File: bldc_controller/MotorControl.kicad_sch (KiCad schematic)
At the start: 10 parts, among them U10 DRV8353FS

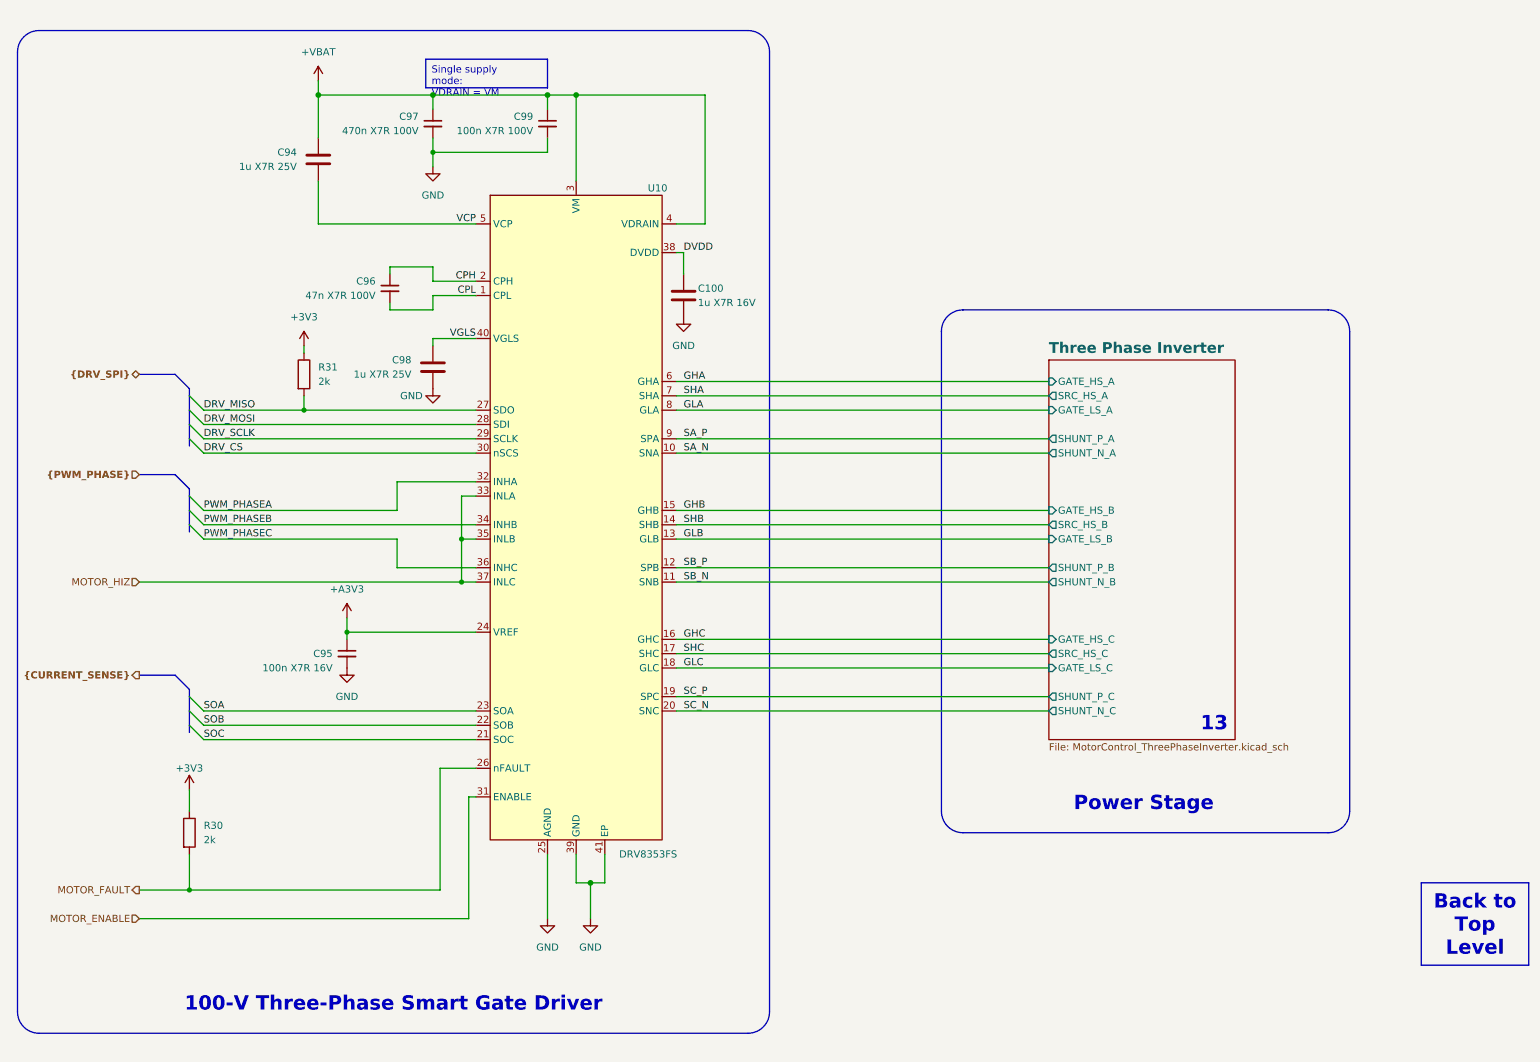
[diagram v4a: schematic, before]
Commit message: Added TVS diodes to all interfaces
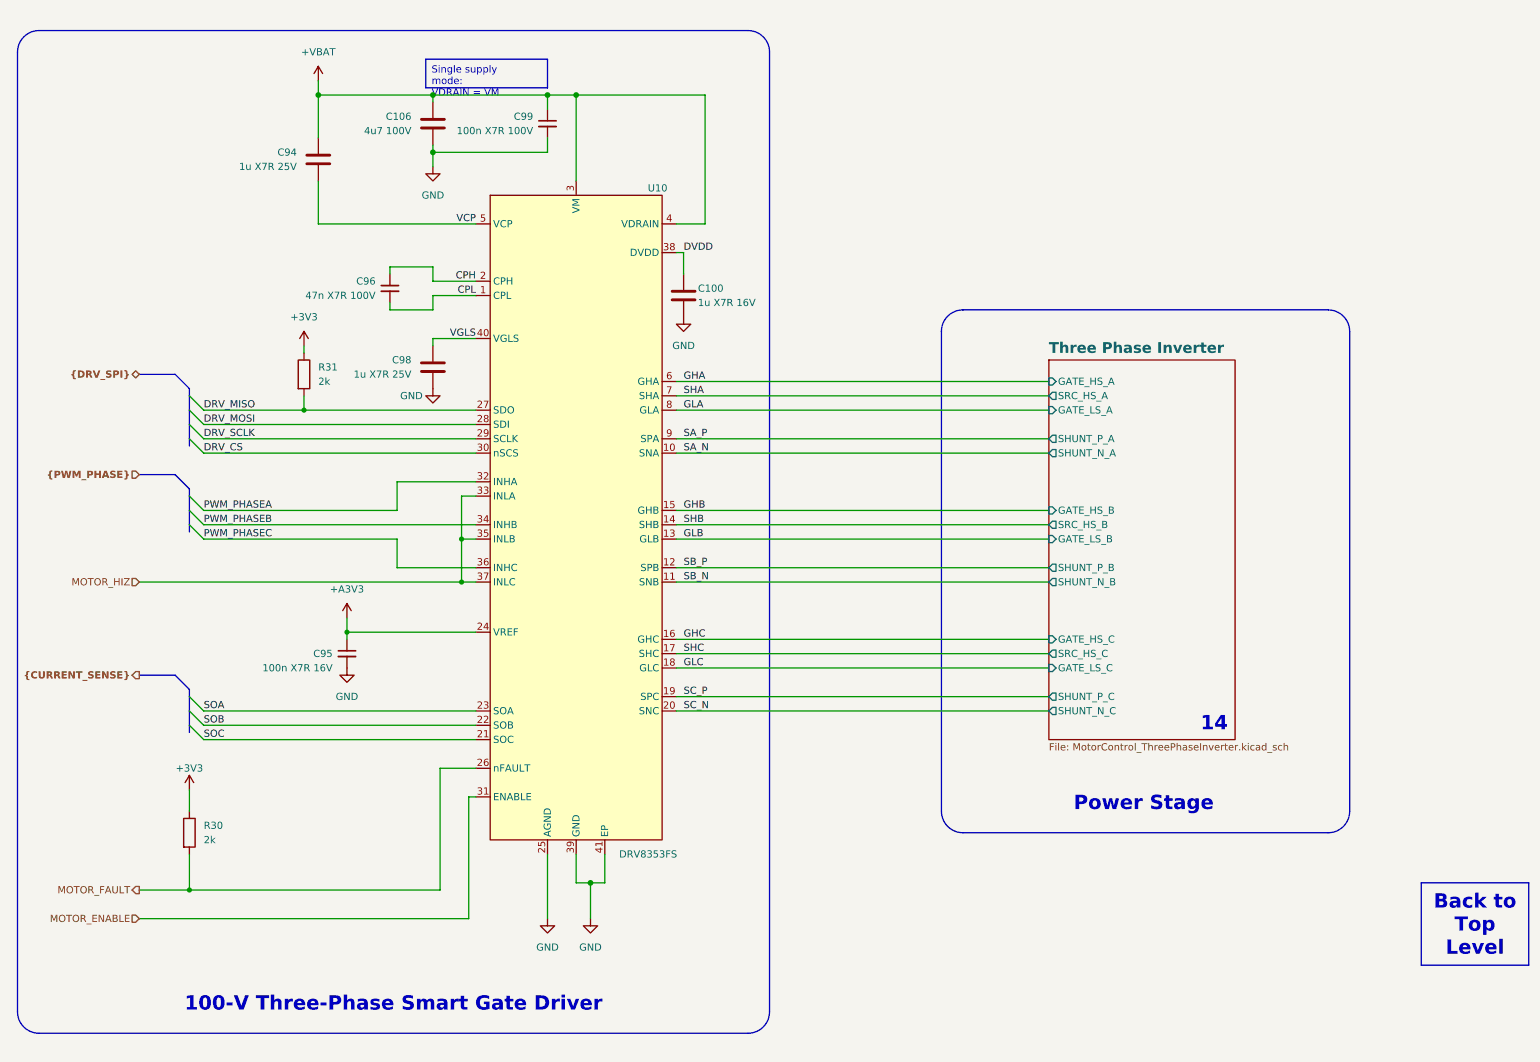
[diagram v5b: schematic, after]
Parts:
- removed C97: 470n X7R 100V, 0_capacitor_smd:C_0402_1005_DensityHigh, symbol Device:C_Small
- added C106: 4u7 100V, 0_capacitor_smd:C_1206_3216_DensityHighest, symbol Device:C
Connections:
- net +VBAT: now also C106.1
- net GND: now also C106.2
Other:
- note added: "14"
- note removed: "13"
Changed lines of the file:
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@@
     (comment 3 "Author: Vincent Nguyen")
   )
+  (junction (at 90.17 36.83) (diameter 1.016) (color 0 0 0 1)
+  )
   (junction (at 110.49 26.67) (diameter 1.016) (color 200 50 50 1)
   )
+  (junction (at 90.17 26.67) (diameter 1.016) (color 200 50 50 1)
+  )
   (junction (at 115.57 26.67) (diameter 1.016) (color 200 50 50 1)
   )
-  (junction (at 90.17 36.83) (diameter 0) (color 0 0 0 1)
-  )
   (junction (at 118.11 166.37) (diameter 1.016) (color 0 0 0 1)
   )
@@
   )
   (junction (at 74.93 121.92) (diameter 0) (color 0 0 0 0)
-  )
-  (junction (at 90.17 26.67) (diameter 1.016) (color 200 50 50 1)
   )
   (junction (at 95.25 105.41) (diameter 0) (color 0 0 0 0)
@@
     (stroke (width 0) (type default))
   )
-  (wire (pts (xy 90.17 36.83) (xy 90.17 34.29))
-    (stroke (width 0.381) (type default) (color 0 0 0 1))
-  )
   (wire (pts (xy 46.99 161.29) (xy 46.99 167.64))
     (stroke (width 0) (type default))
+  )
+  (wire (pts (xy 90.17 26.67) (xy 90.17 27.94))
+    (stroke (width 0.381) (type default) (color 200 50 50 1))
   )
   (wire (pts (xy 96.52 172.72) (xy 96.52 151.13))
@@
     (stroke (width 0) (type default))
   )
-  (wire (pts (xy 90.17 26.67) (xy 90.17 29.21))
+  (wire (pts (xy 90.17 26.67) (xy 110.49 26.67))
     (stroke (width 0.381) (type default) (color 200 50 50 1))
   )
@@
     (stroke (width 0) (type default))
   )
-  (wire (pts (xy 69.85 26.67) (xy 90.17 26.67))
-    (stroke (width 0.381) (type default) (color 200 50 50 1))
+  (wire (pts (xy 90.17 36.83) (xy 90.17 35.56))
+    (stroke (width 0.381) (type default) (color 0 0 0 1))
   )
   (wire (pts (xy 49.53 90.17) (xy 97.79 90.17))
@@
     (stroke (width 0) (type default))
   )
-  (wire (pts (xy 90.17 39.37) (xy 90.17 36.83))
+  (wire (pts (xy 90.17 36.83) (xy 90.17 39.37))
     (stroke (width 0.381) (type default) (color 0 0 0 1))
   )
@@
     (stroke (width 0) (type default))
   )
-  (wire (pts (xy 90.17 26.67) (xy 110.49 26.67))
+  (wire (pts (xy 69.85 26.67) (xy 90.17 26.67))
     (stroke (width 0.381) (type default) (color 200 50 50 1))
   )
@@
     (effects (font (size 2.54 2.54) (thickness 0.508) bold (color 0 0 0 1)) (justify bottom))
   )
-  (text "13" (at 231.14 139.7 0)
-    (effects (font (size 2.54 2.54) bold (color 100 30 50 1)) (justify right bottom) (href "#13"))
+  (text "14" (at 231.14 139.7 0)
+    (effects (font (size 2.54 2.54) bold (color 100 30 50 1)) (justify right bottom) (href "#14"))
   )
   (label "DRV_MOSI" (at 49.53 85.09 0) (fields_autoplaced)
@@
         (path "/0650c7a8-acba-429c-9f8e-eec0baf0bc1c/a6223e2e-2896-4182-b4ad-55a63bc87f3d"
           (reference "#PWR061") (unit 1)
+        )
+      )
+    )
+  )
+  (symbol (lib_id "Device:C") (at 90.17 31.75 0) (mirror y) (unit 1)
+    (in_bom yes) (on_board yes) (dnp no)
+    (property "Reference" "C106" (at 86.36 30.48 0)
+      (effects (font (size 1.27 1.27)) (justify left))
+    )
+    (property "Value" "4u7 100V" (at 86.36 33.02 0)
+      (effects (font (size 1.27 1.27)) (justify left))
+    )
+    (property "Footprint" "0_capacitor_smd:C_1206_3216_DensityHighest" (at 89.2048 35.56 0)
+      (effects (font (size 1.27 1.27)) hide)
+    )
+    (property "Datasheet" "~" (at 90.17 31.75 0)
+      (effects (font (size 1.27 1.27)) hide)
+    )
+    (pin "1")
+    (pin "2")
+    (instances
+      (project "bldc_controller"
+        (path "/0650c7a8-acba-429c-9f8e-eec0baf0bc1c/a6223e2e-2896-4182-b4ad-55a63bc87f3d/4a9c9b06-3536-46ef-a76d-6cac03a1fe38"
+          (reference "C106") (unit 1)
+        )
+        (path "/0650c7a8-acba-429c-9f8e-eec0baf0bc1c/a6223e2e-2896-4182-b4ad-55a63bc87f3d"
+          (reference "C97") (unit 1)
         )
       )
@@
     )
   )
-  (symbol (lib_id "Device:C_Small") (at 90.17 31.75 0) (mirror y) (unit 1)
-    (in_bom yes) (on_board yes) (dnp no)
-    (property "Reference" "C97" (at 87.63 30.48 0)
-      (effects (font (size 1.27 1.27)) (justify left))
-    )
-    (property "Value" "470n X7R 100V" (at 87.63 33.02 0)
-      (effects (font (size 1.27 1.27)) (justify left))
-    )
-    (property "Footprint" "0_capacitor_smd:C_0402_1005_DensityHigh" (at 90.17 31.75 0)
-      (effects (font (size 1.27 1.27)) hide)
-    )
-    (property "Datasheet" "~" (at 90.17 31.75 0)
-      (effects (font (size 1.27 1.27)) hide)
-    )
-    (pin "1")
-    (pin "2")
-    (instances
-      (project "bldc_controller"
-        (path "/0650c7a8-acba-429c-9f8e-eec0baf0bc1c/a6223e2e-2896-4182-b4ad-55a63bc87f3d"
-          (reference "C97") (unit 1)
-        )
-      )
-    )
-  )
   (symbol (lib_id "Device:R") (at 67.31 76.2 0) (unit 1)
     (in_bom yes) (on_board yes) (dnp no) (fields_autoplaced)
@@
     (instances
       (project "bldc_controller"
-        (path "/0650c7a8-acba-429c-9f8e-eec0baf0bc1c/a6223e2e-2896-4182-b4ad-55a63bc87f3d" (page "13"))
-      )
-    )
+        (path "/0650c7a8-acba-429c-9f8e-eec0baf0bc1c/a6223e2e-2896-4182-b4ad-55a63bc87f3d" (page "14"))
+      )
+    )

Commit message: might have fixed net issue, added dxf and svgs
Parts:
- renumbered C106 to C97
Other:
- sheet Three Phase Inverter renamed Motor Control - Inverter
- note added: "Page 9"
- note removed: "14"
- moved on the sheet: C100, C94, C95, C96, C97, C98, C99, R30, R31, U10

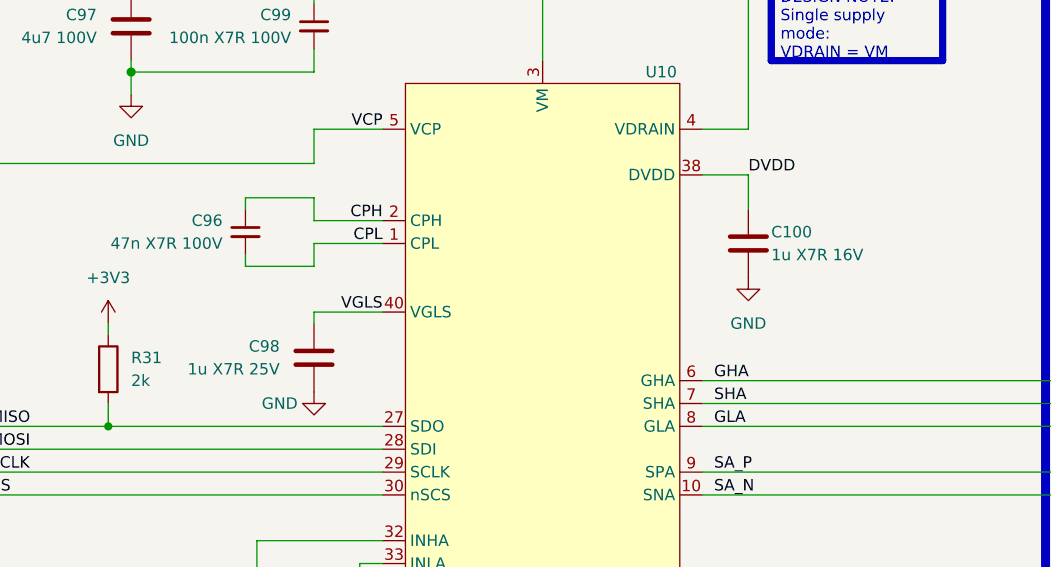
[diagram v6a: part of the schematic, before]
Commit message: added chassis connection to connector MP. Might need to change design rules to be compatible with low-cost PCBWay
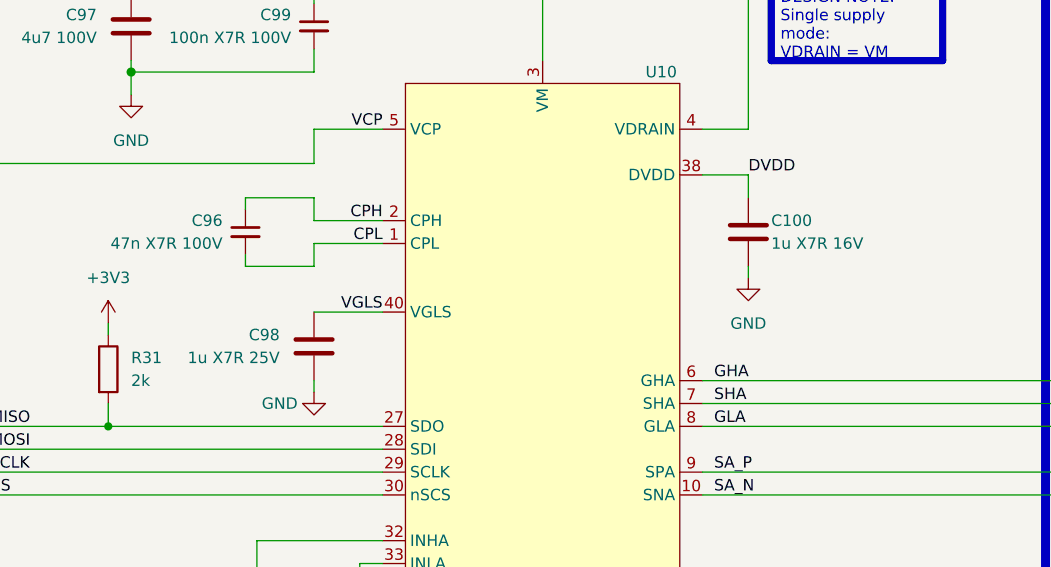
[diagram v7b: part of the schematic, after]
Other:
- moved on the sheet: C100, C98
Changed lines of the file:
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@@
     (stroke (width 0) (type default))
+  )
+  (wire (pts (xy 138.43 72.39) (xy 138.43 73.66))
+    (stroke (width 0.381) (type default) (color 0 0 0 1))
   )
   (wire (pts (xy 49.53 60.96) (xy 90.17 60.96))
@@
   )
   (wire (pts (xy 110.49 168.91) (xy 110.49 173.99))
-    (stroke (width 0) (type default))
+    (stroke (width 0.381) (type default) (color 0 0 0 1))
   )
   (wire (pts (xy 46.99 165.1) (xy 46.99 168.91))
@@
     (stroke (width 0.381) (type default) (color 200 50 50 1))
   )
-  (wire (pts (xy 138.43 66.04) (xy 138.43 62.23))
+  (wire (pts (xy 138.43 64.77) (xy 138.43 62.23))
     (stroke (width 0) (type default))
   )
@@
     (stroke (width 0) (type default))
   )
-  (wire (pts (xy 90.17 78.74) (xy 90.17 77.47))
-    (stroke (width 0) (type default))
-  )
   (wire (pts (xy 82.55 64.77) (xy 82.55 66.04))
     (stroke (width 0) (type default))
@@
   (bus (pts (xy 46.99 140.97) (xy 46.99 143.51))
     (stroke (width 0) (type default))
+  )
+  (wire (pts (xy 90.17 85.09) (xy 90.17 86.36))
+    (stroke (width 0.381) (type default) (color 0 0 0 1))
   )
   (bus (pts (xy 44.45 101.6) (xy 38.1 101.6))
@@
     )
   )
-  (symbol (lib_id "Device:C") (at 90.17 82.55 0) (mirror y) (unit 1)
+  (symbol (lib_id "Device:C") (at 90.17 81.28 0) (mirror y) (unit 1)
     (in_bom yes) (on_board yes) (dnp no)
-    (property "Reference" "C98" (at 86.36 81.28 0)
-      (effects (font (size 1.27 1.27)) (justify left))
-    )
-    (property "Value" "1u X7R 25V" (at 86.36 83.82 0)
-      (effects (font (size 1.27 1.27)) (justify left))
-    )
-    (property "Footprint" "0_capacitor_smd:C_0402_1005_DensityHigh" (at 89.2048 86.36 0)
-      (effects (font (size 1.27 1.27)) hide)
-    )
-    (property "Datasheet" "~" (at 90.17 82.55 0)
+    (property "Reference" "C98" (at 86.36 80.01 0)
+      (effects (font (size 1.27 1.27)) (justify left))
+    )
+    (property "Value" "1u X7R 25V" (at 86.36 82.55 0)
+      (effects (font (size 1.27 1.27)) (justify left))
+    )
+    (property "Footprint" "0_capacitor_smd:C_0402_1005_DensityHigh" (at 89.2048 85.09 0)
+      (effects (font (size 1.27 1.27)) hide)
+    )
+    (property "Datasheet" "~" (at 90.17 81.28 0)
       (effects (font (size 1.27 1.27)) hide)
     )
@@
     )
   )
-  (symbol (lib_id "Device:C") (at 138.43 69.85 0) (unit 1)
+  (symbol (lib_id "Device:C") (at 138.43 68.58 0) (unit 1)
     (in_bom yes) (on_board yes) (dnp no)
-    (property "Reference" "C100" (at 140.97 68.58 0)
-      (effects (font (size 1.27 1.27)) (justify left))
-    )
-    (property "Value" "1u X7R 16V" (at 140.97 71.12 0)
-      (effects (font (size 1.27 1.27)) (justify left))
-    )
-    (property "Footprint" "0_capacitor_smd:C_0402_1005_DensityHigh" (at 139.3952 73.66 0)
-      (effects (font (size 1.27 1.27)) hide)
-    )
-    (property "Datasheet" "~" (at 138.43 69.85 0)
-      (effects (font (size 1.27 1.27)) hide)
-    )
+    (property "Reference" "C100" (at 140.97 67.31 0)
+      (effects (font (size 1.27 1.27)) (justify left))
+    )
+    (property "Value" "1u X7R 16V" (at 140.97 69.85 0)
+      (effects (font (size 1.27 1.27)) (justify left))
+    )
+    (property "Footprint" "0_capacitor_smd:C_0402_1005_DensityHigh" (at 139.3952 72.39 0)
+      (effects (font (size 1.27 1.27)) hide)
+    )
+    (property "Datasheet" "~" (at 138.43 68.58 0)
+      (effects (font (size 1.27 1.27)) hide)
+    )

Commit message: starting rerouting for PCBWay 8/8 mils, 0.25mm drill
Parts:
- U10: footprint Package_DFN_QFN:HVQFN-40-1EP_6x6mm_P0.5mm_EP4.1x4.1mm_ThermalVias -> 0_package_DFN_QFN:WQFN-40-1EP_6x6mm_P0.5mm_EP4.15x4.15mm_ThermalVias
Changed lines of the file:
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@@
       (effects (font (size 1.27 1.27)) (justify left))
     )
-    (property "Footprint" "Package_DFN_QFN:HVQFN-40-1EP_6x6mm_P0.5mm_EP4.1x4.1mm_ThermalVias" (at 13.97 62.23 0)
+    (property "Footprint" "0_package_DFN_QFN:WQFN-40-1EP_6x6mm_P0.5mm_EP4.15x4.15mm_ThermalVias" (at 13.97 62.23 0)
       (effects (font (size 1.27 1.27)) hide)
     )
